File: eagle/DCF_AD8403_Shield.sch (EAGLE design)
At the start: 21 parts, among them IC1 TL072P, IC2 AD8403-100, J1 DCIN

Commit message: 基板図仮配線
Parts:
- removed JACK1, JACK2: MJ-353W-0, mylib2:MJ-353W-0
- removed JP5: TS_SELECT, pinhead:PINHD-1X3
- added U$1, U$2: AK_RCA_JACK_DIP, mylib2:AK_RCA_JACK_DIP
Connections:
- removed net N$2: JACK1.2, JP5.1
- removed net N$4: JACK1.3, JP5.3
- net AGND: now also U$1.S, U$2.S; no longer JACK1.1, JACK2.1
- net BYPASS: now also U$1.T; no longer JACK2.3
- net FILTERED: now also U$2.T; no longer JACK2.2
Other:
- moved on the sheet: C4, C5, C6, C7, IC1B, J1, JP6, R1, R2

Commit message: Update Eagle Files
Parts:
- removed U$1: AK_RCA_JACK_DIP, mylib2:AK_RCA_JACK_DIP
- added JK1: AK_RCA_JACK_DIP_REVERSE, mylib2:AK_RCA_JACK_DIP_REVERSE
- added LED1: (no value), led:LED3MM
- added R4: 1k, rcl:R-EU_0204/7
- C4, C5: value (none) -> 0.1uF
- C6, C7: value (none) -> 100uF; device rcl:CPOL-EUSANYO_E9 -> rcl:CPOL-EUE2.5-6
- R1, R2: value (none) -> 100k
- R3: value (none) -> 0
- renumbered U$2 to JK2
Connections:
- removed net VDD: C5.1, C6.+, IC1P.V+, J1.1, JP6.1, R1.2
- removed net VSS: C4.2, C7.-, IC1P.V-, J1.3, JP6.2, R2.1
- new net N$2: LED1.A, R4.1
- new net V+: C5.1, C6.+, IC1P.V+, J1.1, JP6.1, R1.2, R4.2
- new net V-: C4.2, C7.-, IC1P.V-, J1.3, JP6.2, LED1.C, R2.1
- net +5V: now also C3.1; no longer C3.2
- net AGND: now also C3.2, JK1.S, R3.1; no longer R3.2, U$1.S
- net BYPASS: now also JK1.T; no longer U$1.T
- net GND: now also R3.2; no longer C3.1, R3.1
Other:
- moved on the sheet: C3, J1, JP6, R3

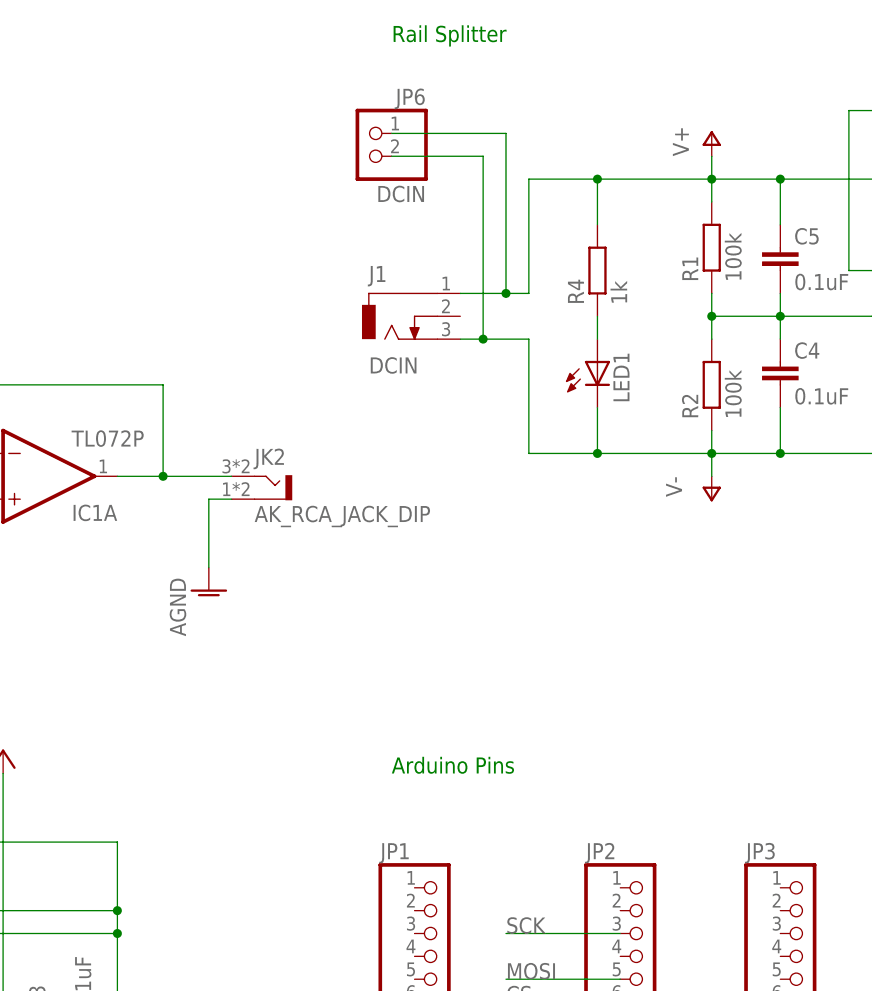
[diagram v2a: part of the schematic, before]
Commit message: Add: output AC Coupling
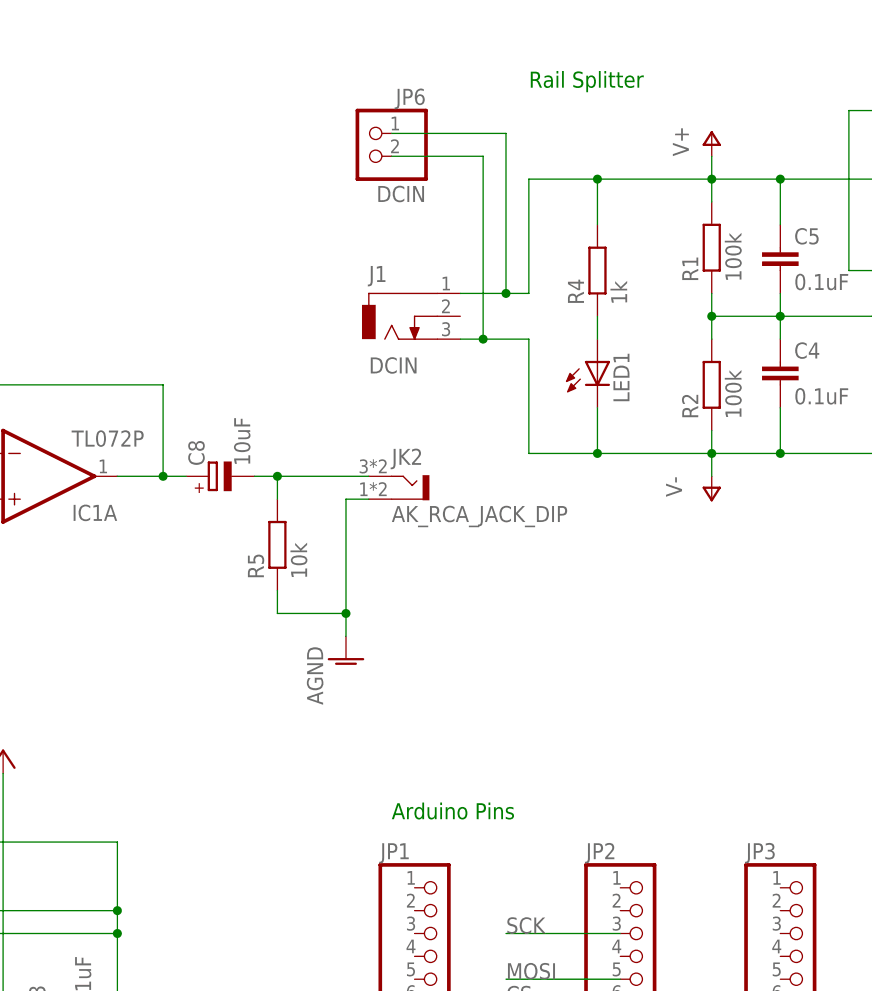
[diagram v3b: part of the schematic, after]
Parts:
- added C8: 10uF, rcl:CPOL-EUE5-6
- added R5: 10k, rcl:R-EU_0204/7
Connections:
- new net N$3: C8.-, JK2.T, R5.2
- net AGND: now also R5.1
- net FILTERED: now also C8.+; no longer JK2.T
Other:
- moved on the sheet: JK2
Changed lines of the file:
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@@
 <setting verticaltext="up"/>
 </settings>
-<grid distance="0.1" unitdist="inch" unit="inch" style="lines" multiple="1" display="no" altdistance="0.01" altunitdist="inch" altunit="inch"/>
+<grid distance="0.1" unitdist="inch" unit="inch" style="lines" multiple="1" display="yes" altdistance="0.01" altunitdist="inch" altunit="inch"/>
 <layers>
 <layer number="1" name="Top" color="4" fill="1" visible="no" active="no"/>
@@
 <part name="AGND6" library="supply1" deviceset="AGND" device=""/>
 <part name="AGND7" library="supply1" deviceset="AGND" device=""/>
+<part name="C8" library="rcl" deviceset="CPOL-EU" device="E5-6" value="10uF"/>
+<part name="R5" library="rcl" deviceset="R-EU_" device="0204/7" value="10k"/>
 </parts>
 <sheets>
 <sheet>
 <plain>
-<text x="152.4" y="162.56" size="1.778" layer="91">Rail Splitter</text>
-<text x="152.4" y="81.28" size="1.778" layer="91">Arduino Pins</text>
+<text x="167.64" y="157.48" size="1.778" layer="91">Rail Splitter</text>
+<text x="152.4" y="76.2" size="1.778" layer="91">Arduino Pins</text>
 </plain>
 <instances>
@@
 <instance part="FRAME1" gate="G$1" x="0" y="0"/>
 <instance part="JK1" gate="G$1" x="40.64" y="111.76" rot="MR0"/>
-<instance part="JK2" gate="G$1" x="137.16" y="114.3"/>
+<instance part="JK2" gate="G$1" x="152.4" y="114.3"/>
 <instance part="R3" gate="G$1" x="218.44" y="60.96"/>
 <instance part="LED1" gate="G$1" x="175.26" y="127"/>
@@
 <instance part="P-1" gate="1" x="187.96" y="111.76"/>
 <instance part="AGND1" gate="VR1" x="45.72" y="96.52"/>
-<instance part="AGND2" gate="VR1" x="132.08" y="101.6"/>
+<instance part="AGND2" gate="VR1" x="147.32" y="93.98"/>
 <instance part="AGND3" gate="VR1" x="48.26" y="35.56"/>
 <instance part="AGND4" gate="VR1" x="121.92" y="35.56"/>
@@
 <instance part="AGND6" gate="VR1" x="238.76" y="127"/>
 <instance part="AGND7" gate="VR1" x="73.66" y="96.52"/>
+<instance part="C8" gate="G$1" x="132.08" y="114.3" rot="R90"/>
+<instance part="R5" gate="G$1" x="139.7" y="106.68" rot="R90"/>
 </instances>
 <busses>
@@
 <wire x1="96.52" y1="71.12" x2="96.52" y2="124.46" width="0.1524" layer="91"/>
 <junction x="96.52" y="124.46"/>
-<wire x1="127" y1="114.3" x2="134.62" y2="114.3" width="0.1524" layer="91"/>
+<pinref part="C8" gate="G$1" pin="+"/>
+<wire x1="129.54" y1="114.3" x2="127" y2="114.3" width="0.1524" layer="91"/>
 <junction x="127" y="114.3"/>
-<pinref part="JK2" gate="G$1" pin="T"/>
 </segment>
 </net>
@@
 </segment>
 <segment>
-<wire x1="132.08" y1="104.14" x2="132.08" y2="111.76" width="0.1524" layer="91"/>
+<wire x1="147.32" y1="96.52" x2="147.32" y2="99.06" width="0.1524" layer="91"/>
 <pinref part="JK2" gate="G$1" pin="S"/>
-<wire x1="134.62" y1="111.76" x2="132.08" y2="111.76" width="0.1524" layer="91"/>
+<wire x1="147.32" y1="99.06" x2="147.32" y2="111.76" width="0.1524" layer="91"/>
+<wire x1="149.86" y1="111.76" x2="147.32" y2="111.76" width="0.1524" layer="91"/>
 <pinref part="AGND2" gate="VR1" pin="AGND"/>
+<pinref part="R5" gate="G$1" pin="1"/>
+<wire x1="139.7" y1="101.6" x2="139.7" y2="99.06" width="0.1524" layer="91"/>
+<wire x1="139.7" y1="99.06" x2="147.32" y2="99.06" width="0.1524" layer="91"/>
+<junction x="147.32" y="99.06"/>
 </segment>
 <segment>
@@
 </segment>
 </net>
+<net name="N$3" class="0">
+<segment>
+<pinref part="C8" gate="G$1" pin="-"/>
+<pinref part="JK2" gate="G$1" pin="T"/>
+<wire x1="137.16" y1="114.3" x2="139.7" y2="114.3" width="0.1524" layer="91"/>
+<pinref part="R5" gate="G$1" pin="2"/>
+<wire x1="139.7" y1="114.3" x2="149.86" y2="114.3" width="0.1524" layer="91"/>
+<wire x1="139.7" y1="111.76" x2="139.7" y2="114.3" width="0.1524" layer="91"/>
+<junction x="139.7" y="114.3"/>
+</segment>
+</net>

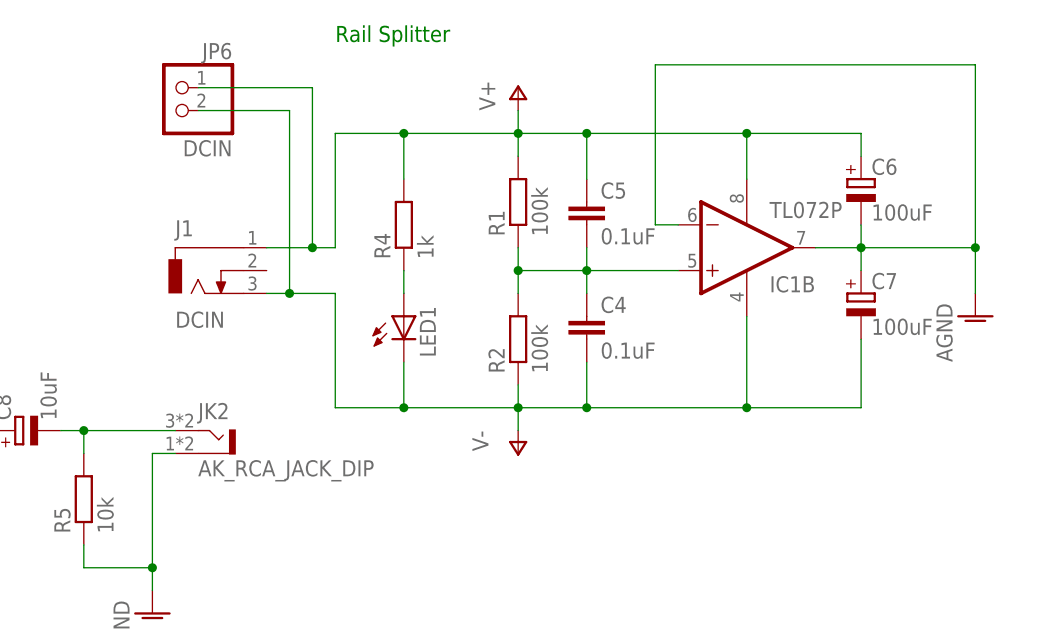
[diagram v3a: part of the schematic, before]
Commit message: Remove: Decoupling Capacitor of OPAMP
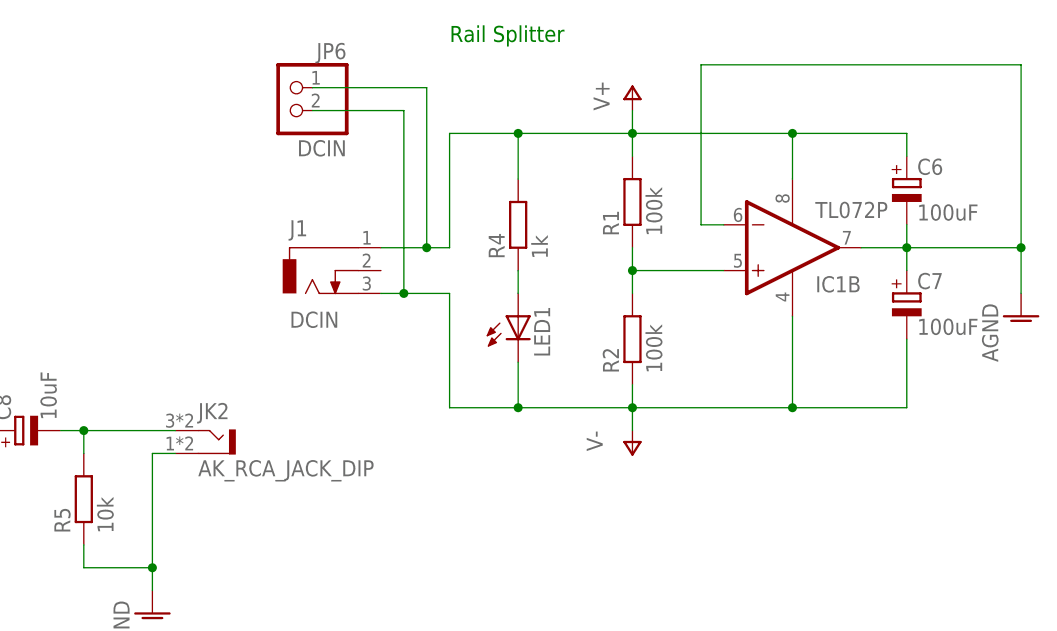
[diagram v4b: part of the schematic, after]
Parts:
- removed C4, C5: 0.1uF, rcl:C-EU025-024X044
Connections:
- net N$5: no longer C4.1, C5.2
- net V+: no longer C5.1
- net V-: no longer C4.2
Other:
- moved on the sheet: C6, C7, IC1B, J1, JP6, LED1, R1, R2, R4

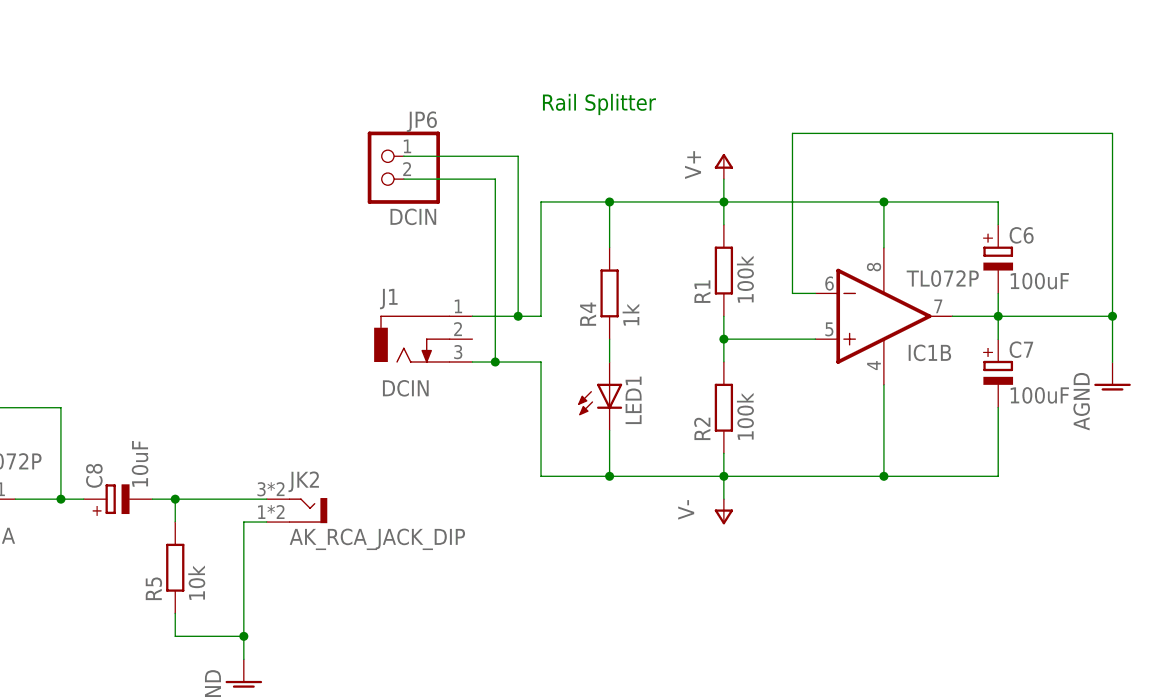
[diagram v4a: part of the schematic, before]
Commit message: Add: OPAMP Decoupling Capacitor
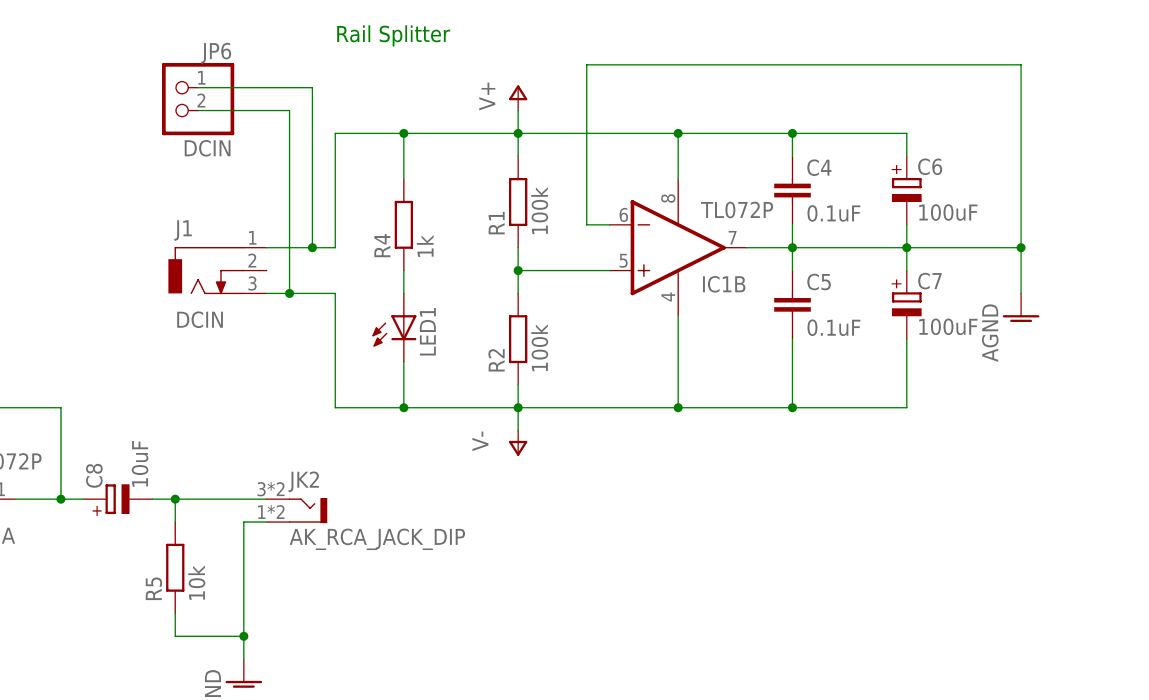
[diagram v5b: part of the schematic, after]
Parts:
- added C4, C5: 0.1uF, rcl:C-EU025-024X044
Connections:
- net AGND: now also C4.2, C5.1
- net V+: now also C4.1
- net V-: now also C5.2
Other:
- moved on the sheet: C6, C7, IC1B, J1, JP6, LED1, R1, R2, R4

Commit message: 配線完了
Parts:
- removed J1: DCIN, con-jack:DCJ0303
- removed JP6: DCIN, pinhead:PINHD-1X2
- removed R3: 0, rcl:R-EU_0207/7
- C1, C2: device rcl:C-EU075-032X103 -> rcl:C-EU050-030X075
- IC1: value TL072P -> NJM2732
- LED1: value (none) -> GREEN
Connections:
- removed net AGND: C2.2, C3.2, C4.2, C5.1, C6.-, C7.+, IC1B.-IN, IC1B.OUT, IC2.1, IC2.17, IC2.20, IC2.21, IC2.24, IC2.5, JK1.S, JK2.S, R3.1, R5.1
- removed net V+: C4.1, C6.+, IC1P.V+, J1.1, JP6.1, R1.2, R4.2
- removed net V-: C5.2, C7.-, IC1P.V-, J1.3, JP6.2, LED1.C, R2.1
- new net N$10: C2.2, C4.2, C5.1, C6.-, C7.+, IC1B.-IN, IC1B.OUT, IC2.21, JK1.S, JK2.S, R5.1
- net +5V: now also C4.1, C6.+, IC1P.V+, R1.2, R4.2
- net GND: now also C3.2, C5.2, C7.-, IC1P.V-, IC2.1, IC2.17, IC2.20, IC2.24, IC2.5, JP4.5, LED1.C, R2.1; no longer R3.2

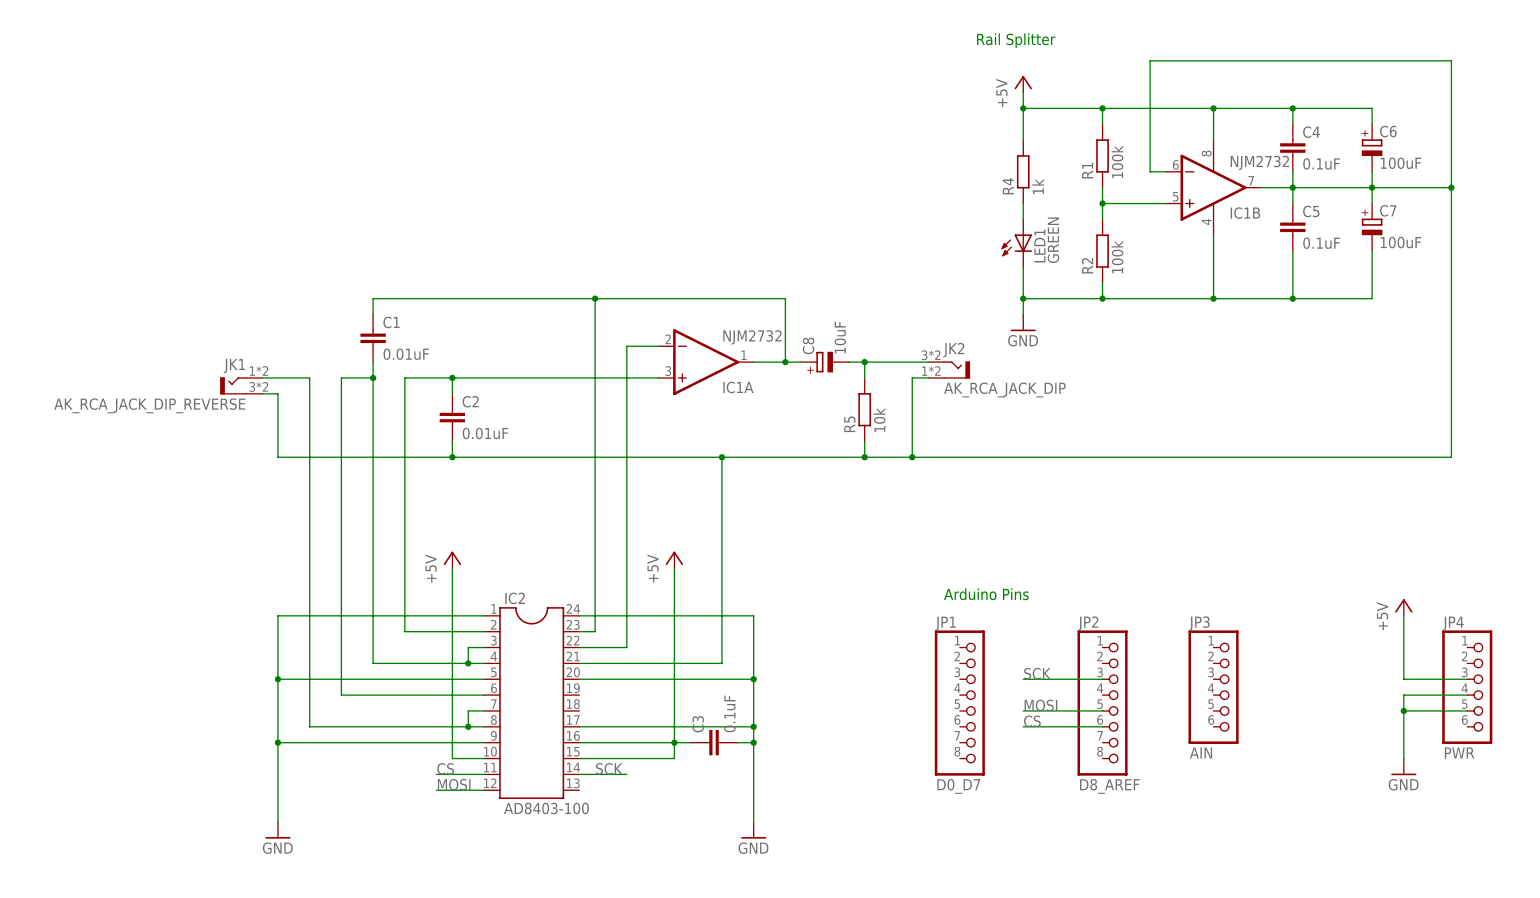
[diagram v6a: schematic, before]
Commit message: Add: Input trim pot
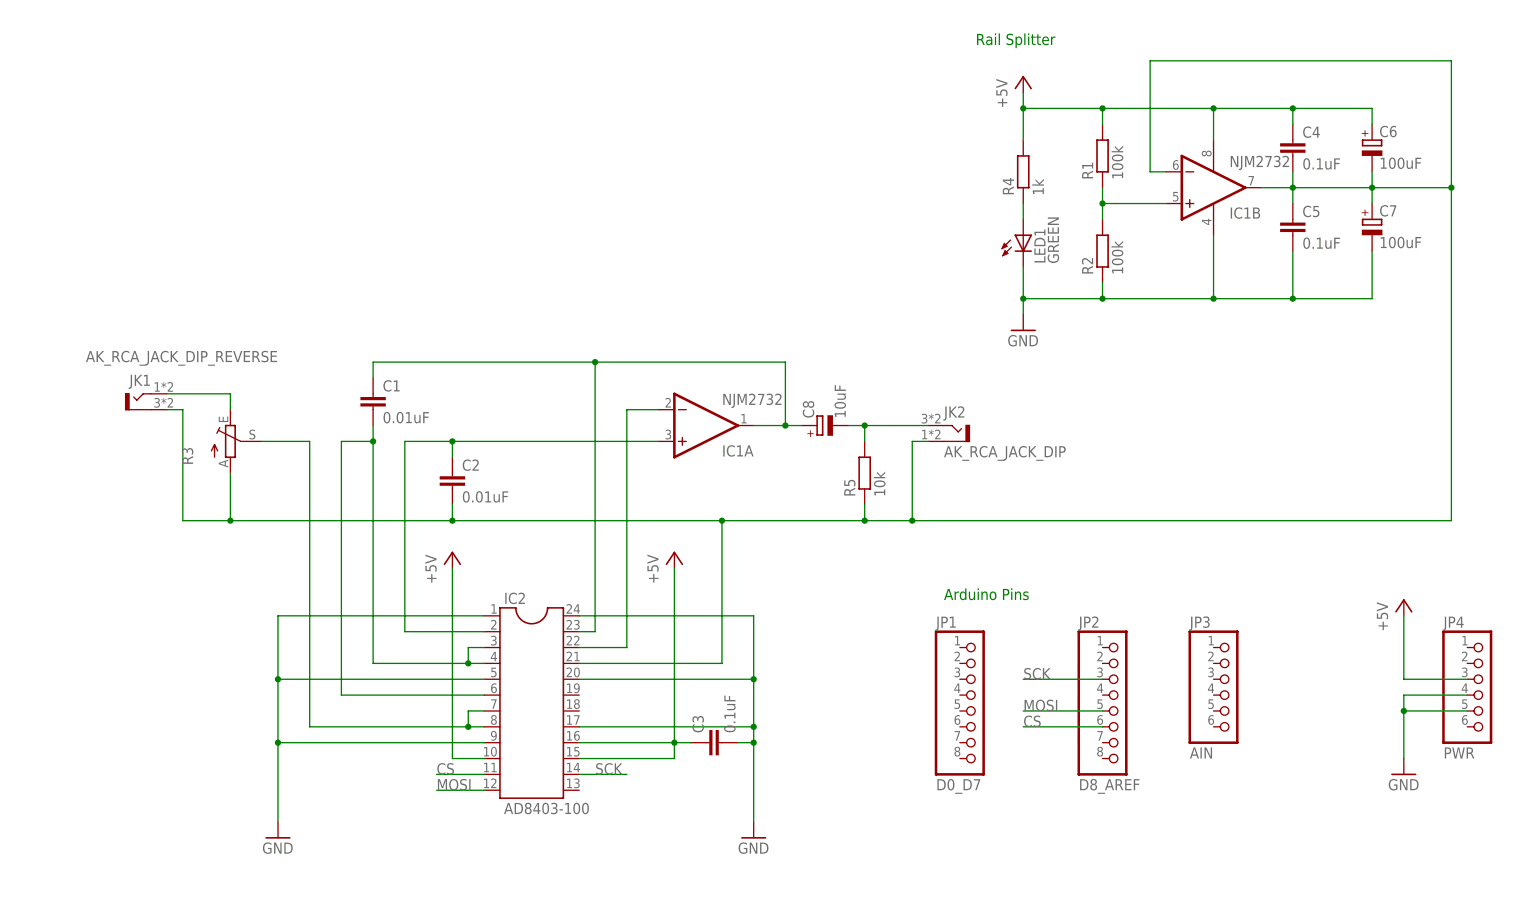
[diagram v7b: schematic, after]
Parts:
- added R3: (no value), pot:TRIM_EU-B25P
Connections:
- new net N$7: JK1.T, R3.E
- net BYPASS: now also R3.S; no longer JK1.T
- net N$10: now also R3.A
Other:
- moved on the sheet: C1, C2, C8, IC1A, JK1, JK2, R5
